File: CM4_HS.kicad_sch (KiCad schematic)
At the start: 6 parts, among them J1801 I2C EN, J1802 CM4/5 Module B

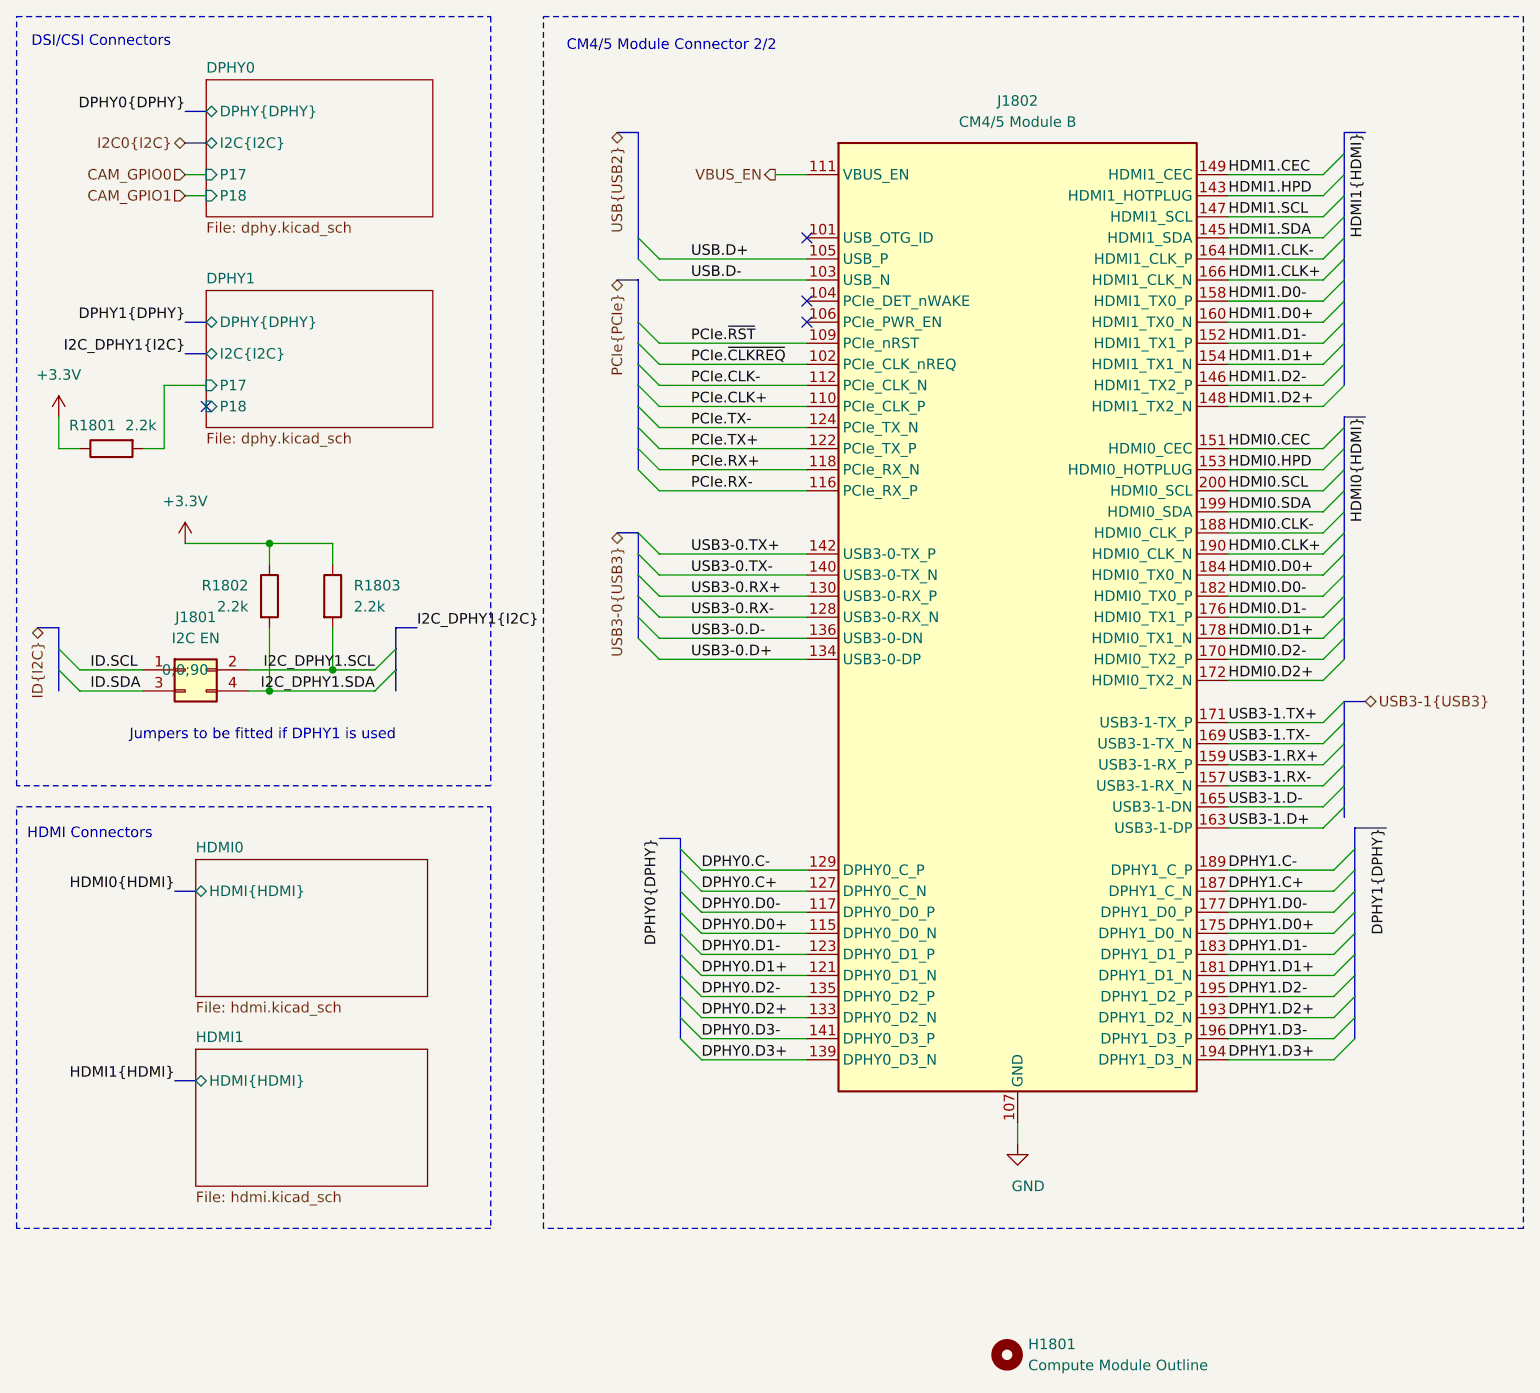
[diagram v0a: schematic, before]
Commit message: Replace DPHY selector jumper with a slide switch
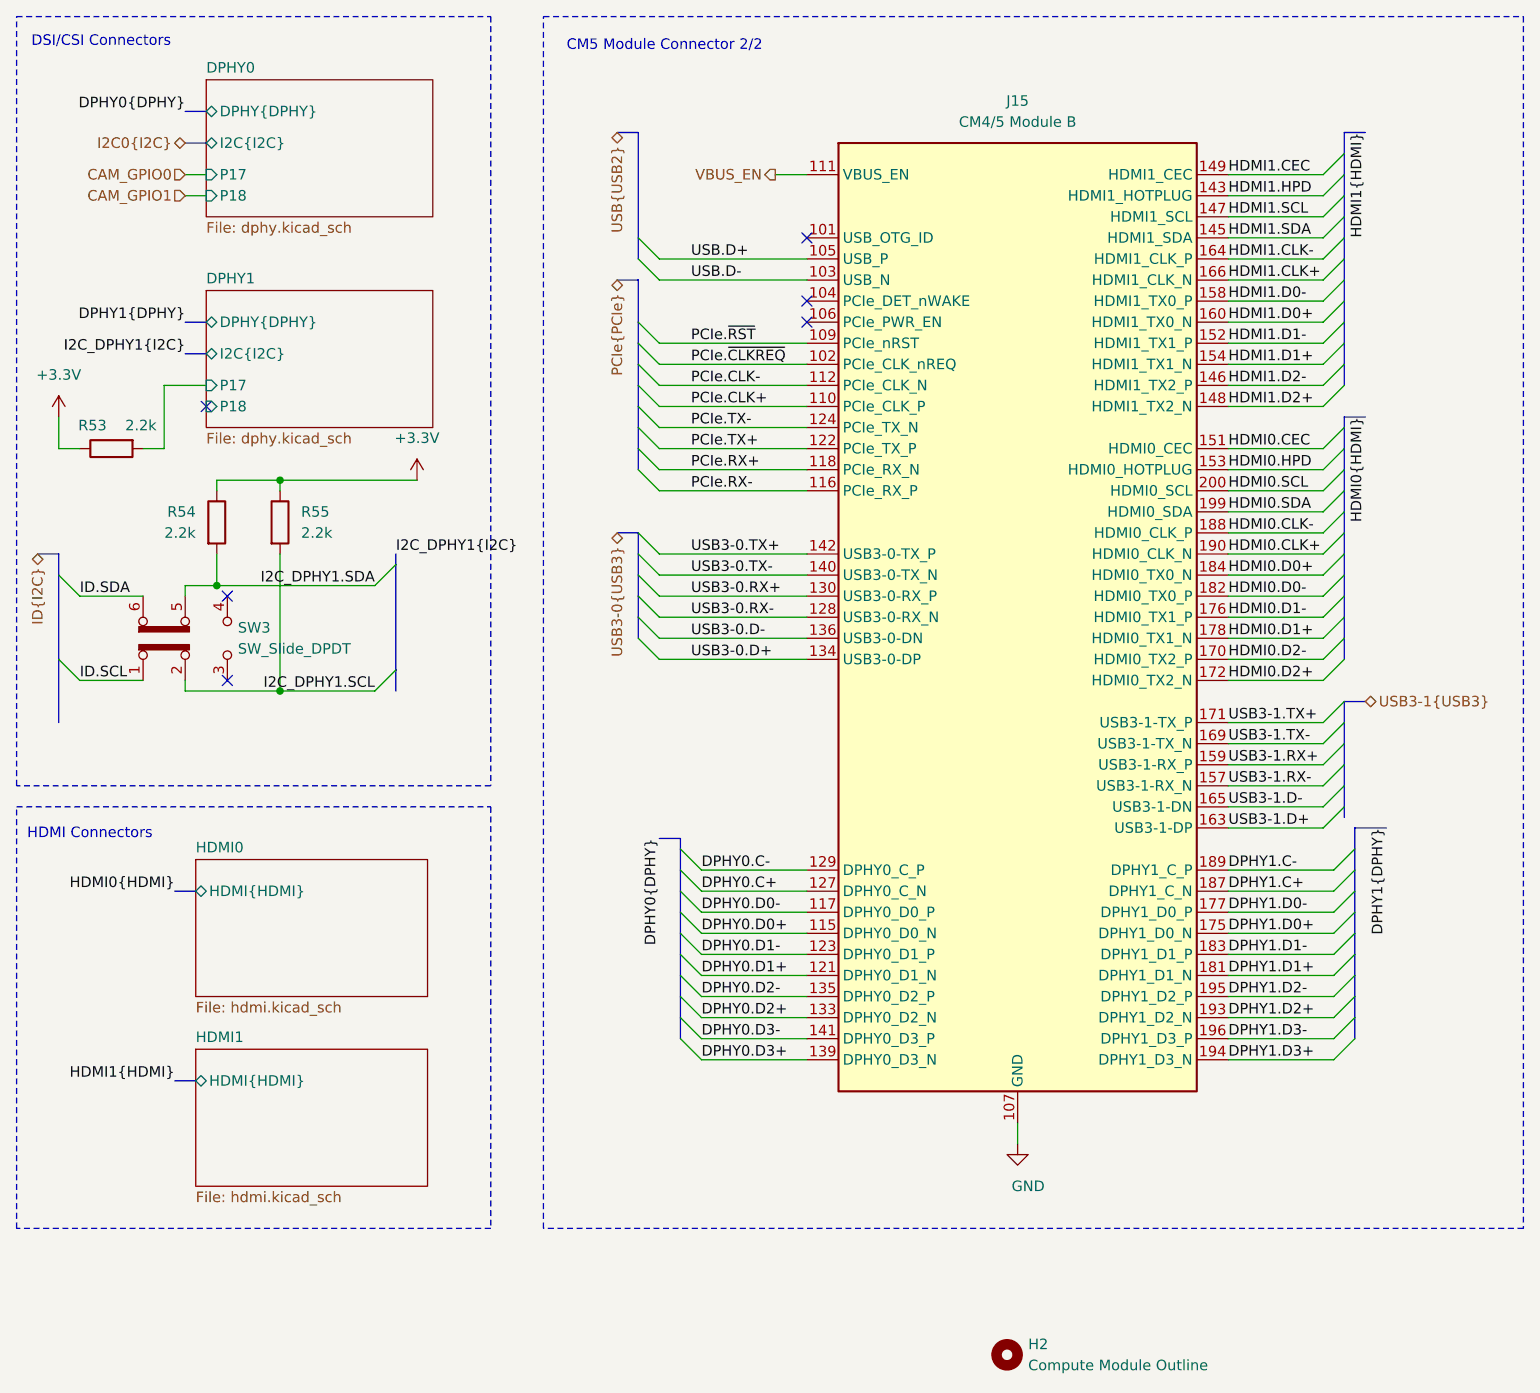
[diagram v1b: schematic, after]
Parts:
- removed J1801: I2C EN, Connector_PinHeader_2.54mm:PinHeader_2x02_P2.54mm_Vertical_SMD, symbol Connector_Generic:Conn_02x02_Odd_Even
- added SW3: SW_Slide_DPDT, HL_Button_Switch:SW-SMD_HX-MSS22C02-HXX-125, symbol Switch:SW_Slide_DPDT
- renumbered H1801 to H2, J1802 to J15, R1801 to R53, R1802 to R54, R1803 to R55
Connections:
- net I2C_DPHY1.SCL: now also SW3.2 (B)
- net I2C_DPHY1.SDA: now also SW3.5 (B)
- net ID.SCL: now also SW3.1 (A)
- net ID.SDA: now also SW3.6 (C)
- no-connect marks 4 -> 6
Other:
- note added: "CM5 Module Connector 2/2"
- note removed: "CM4/5 Module Connector 2/2"
- note removed: "Jumpers to be fitted if DPHY1 is used"
- moved on the sheet: R54, R55

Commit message: Reannotate the board
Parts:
- renumbered J15 to J14
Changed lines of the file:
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@@
+		(polyline
+			(pts
+				(xy 107.95 76.2) (xy 107.95 93.98) (xy 105.41 93.98) (xy 105.41 76.2)
+			)
+			(stroke
+				(width 0)
+				(type dash)
+			)
+			(fill
+				(type none)
+			)
+		)
+	)
+	(rule_area
 		(polyline
 			(pts
@@
 		(polyline
 			(pts
+				(xy 166.37 76.2) (xy 166.37 96.52) (xy 163.83 96.52) (xy 163.83 76.2)
+			)
+			(stroke
+				(width 0)
+				(type dash)
+			)
+			(fill
+				(type none)
+			)
+		)
+	)
+	(rule_area
+		(polyline
+			(pts
 				(xy 163.83 97.79) (xy 163.83 114.3) (xy 166.37 114.3) (xy 166.37 97.79)
+			)
+			(stroke
+				(width 0)
+				(type dash)
+			)
+			(fill
+				(type none)
+			)
+		)
+	)
+	(rule_area
+		(polyline
+			(pts
+				(xy 107.95 113.03) (xy 107.95 143.51) (xy 105.41 143.51) (xy 105.41 113.03)
+			)
+			(stroke
+				(width 0)
+				(type dash)
+			)
+			(fill
+				(type none)
+			)
+		)
+	)
+	(rule_area
+		(polyline
+			(pts
+				(xy 163.83 64.77) (xy 166.37 64.77) (xy 166.37 76.2) (xy 163.83 76.2)
+			)
+			(stroke
+				(width 0)
+				(type dash)
+			)
+			(fill
+				(type none)
+			)
+		)
+	)
+	(rule_area
+		(polyline
+			(pts
+				(xy 107.95 58.42) (xy 107.95 73.66) (xy 105.41 73.66) (xy 105.41 58.42)
 			)
 			(stroke
@@
 			(pts
 				(xy 105.41 53.34) (xy 107.95 53.34) (xy 107.95 58.42) (xy 105.41 58.42)
-			)
-			(stroke
-				(width 0)
-				(type dash)
-			)
-			(fill
-				(type none)
-			)
-		)
-	)
-	(rule_area
-		(polyline
-			(pts
-				(xy 163.83 64.77) (xy 166.37 64.77) (xy 166.37 76.2) (xy 163.83 76.2)
-			)
-			(stroke
-				(width 0)
-				(type dash)
-			)
-			(fill
-				(type none)
-			)
-		)
-	)
-	(rule_area
-		(polyline
-			(pts
-				(xy 107.95 76.2) (xy 107.95 93.98) (xy 105.41 93.98) (xy 105.41 76.2)
-			)
-			(stroke
-				(width 0)
-				(type dash)
-			)
-			(fill
-				(type none)
-			)
-		)
-	)
-	(rule_area
-		(polyline
-			(pts
-				(xy 107.95 113.03) (xy 107.95 143.51) (xy 105.41 143.51) (xy 105.41 113.03)
-			)
-			(stroke
-				(width 0)
-				(type dash)
-			)
-			(fill
-				(type none)
-			)
-		)
-	)
-	(rule_area
-		(polyline
-			(pts
-				(xy 107.95 58.42) (xy 107.95 73.66) (xy 105.41 73.66) (xy 105.41 58.42)
-			)
-			(stroke
-				(width 0)
-				(type dash)
-			)
-			(fill
-				(type none)
-			)
-		)
-	)
-	(rule_area
-		(polyline
-			(pts
-				(xy 166.37 76.2) (xy 166.37 96.52) (xy 163.83 96.52) (xy 163.83 76.2)
 			)
 			(stroke
@@
 		(dnp no)
 		(fields_autoplaced yes)
-		(property "Reference" "#PWR0108"
+		(property "Reference" "#PWR0107"
 			(at 20.32 67.31 0)
 			(effects
@@
 			(project ""
 				(path "/abc482bd-3f17-4d35-80db-1da3dcdb5c27/851e7ce4-d5b0-47f7-ace9-4a347f172348"
-					(reference "#PWR0108")
+					(reference "#PWR0107")
 					(unit 1)
 				)
@@
 		(on_board yes)
 		(dnp no)
-		(property "Reference" "#PWR0110"
+		(property "Reference" "#PWR0109"
 			(at 135.89 157.48 0)
 			(effects
@@
 			(project "Yellow"
 				(path "/abc482bd-3f17-4d35-80db-1da3dcdb5c27/851e7ce4-d5b0-47f7-ace9-4a347f172348"
-					(reference "#PWR0110")
+					(reference "#PWR0109")
 					(unit 1)
 				)
@@
 		(dnp no)
 		(fields_autoplaced yes)
-		(property "Reference" "J15"
+		(property "Reference" "J14"
 			(at 135.89 25.4 0)
 			(effects
@@
 			(project ""
 				(path "/abc482bd-3f17-4d35-80db-1da3dcdb5c27/851e7ce4-d5b0-47f7-ace9-4a347f172348"
-					(reference "J15")
+					(reference "J14")
 					(unit 1)
 				)
@@
 		(dnp no)
 		(fields_autoplaced yes)
-		(property "Reference" "#PWR0109"
+		(property "Reference" "#PWR0108"
 			(at 63.5 74.93 0)
 			(effects
@@
 			(project "HALPI2"
 				(path "/abc482bd-3f17-4d35-80db-1da3dcdb5c27/851e7ce4-d5b0-47f7-ace9-4a347f172348"
-					(reference "#PWR0109")
+					(reference "#PWR0108")
 					(unit 1)
 				)

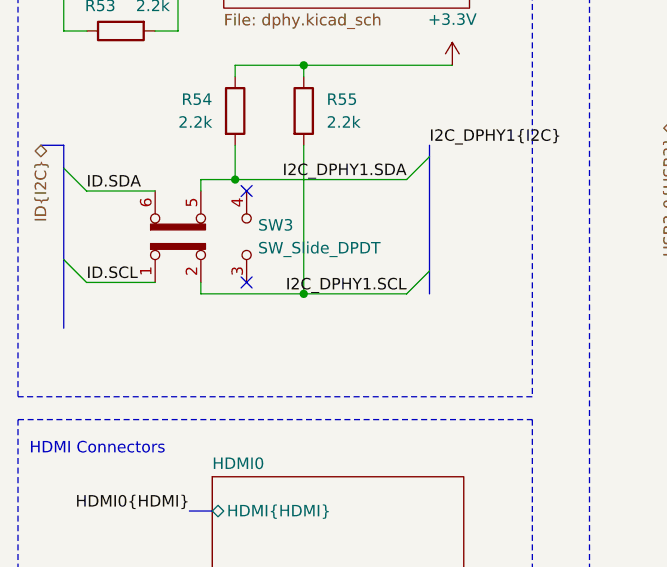
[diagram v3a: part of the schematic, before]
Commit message: Add GND/3.3V/5V headers, add missing JLC part numbers
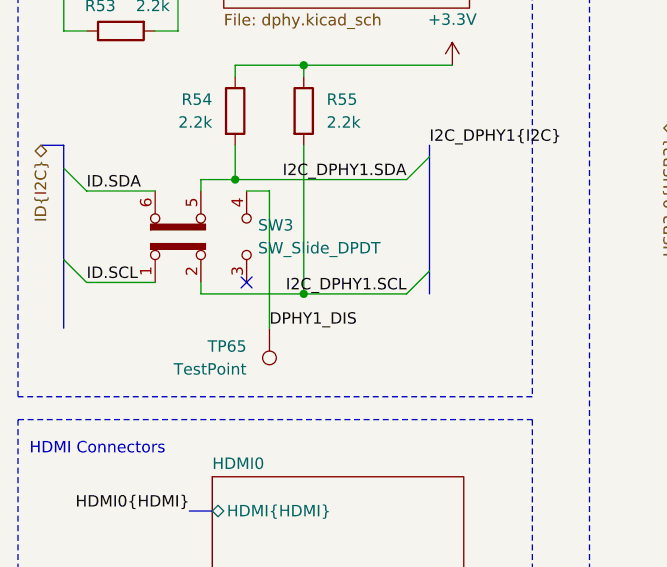
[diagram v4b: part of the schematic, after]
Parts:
- added TP65: TestPoint, TestPoint:TestPoint_Pad_D1.0mm, symbol Connector:TestPoint
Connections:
- net DPHY1_DIS: now reaches SW3.4 (A)
- net DPHY1_DIS: now also TP65.1
- no-connect marks 6 -> 5
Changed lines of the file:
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@@
 	)
 	(no_connect
-		(at 40.64 85.09)
-	)
-	(no_connect
 		(at 40.64 95.25)
 	)
@@
 		)
 	)
+	(wire
+		(pts
+			(xy 43.18 85.09) (xy 40.64 85.09)
+		)
+		(stroke
+			(width 0)
+			(type default)
+		)
+	)
 	(polyline
 		(pts
@@
 	(wire
 		(pts
+			(xy 43.18 100.33) (xy 43.18 85.09)
+		)
+		(stroke
+			(width 0)
+			(type default)
+		)
+	)
+	(wire
+		(pts
 			(xy 161.29 59.69) (xy 172.72 59.69)
 		)
@@
 		)
 	)
+	(label "DPHY1_DIS"
+		(at 43.18 100.33 0)
+		(effects
+			(font
+				(size 1.27 1.27)
+			)
+			(justify left bottom)
+		)
+	)
 	(label "HDMI0{HDMI}"
 		(at 177.8 63.5 270)
@@
 					(unit 1)
 				)
+			)
+		)
+	)
+	(symbol
+		(lib_id "Connector:TestPoint")
+		(at 43.18 100.33 0)
+		(mirror x)
+		(unit 1)
+		(exclude_from_sim no)
+		(in_bom yes)
+		(on_board yes)
+		(dnp no)
+		(fields_autoplaced yes)
+		(property "Reference" "TP65"
+			(at 40.64 102.3619 0)
+			(effects
+				(font
+					(size 1.27 1.27)
+				)
+				(justify right)
+			)
+		)
+		(property "Value" "TestPoint"
+			(at 40.64 104.9019 0)
+			(effects
+				(font
+					(size 1.27 1.27)
+				)
+				(justify right)
+			)
+		)
+		(property "Footprint" "TestPoint:TestPoint_Pad_D1.0mm"
+			(at 48.26 100.33 0)
+			(effects
+				(font
+					(size 1.27 1.27)
+				)
+				(hide yes)
+			)
+		)
+		(property "Datasheet" "~"
+			(at 48.26 100.33 0)
+			(effects
+				(font
+					(size 1.27 1.27)
+				)
+				(hide yes)
+			)
+		)
+		(property "Description" "test point"
+			(at 43.18 100.33 0)
+			(effects
+				(font
+					(size 1.27 1.27)
+				)
+				(hide yes)
+			)
+		)
+		(property "Characteristics" ""
+			(at 43.18 100.33 0)
+			(effects
+				(font
+					(size 1.27 1.27)
+				)
+				(hide yes)
+			)
+		)
+		(property "LCSC Part" ""
+			(at 43.18 100.33 0)
+			(effects
+				(font
+					(size 1.27 1.27)
+				)
+			)
+		)
+		(property "Field8" ""
+			(at 43.18 100.33 0)
+			(effects
+				(font
+					(size 1.27 1.27)
+				)
+			)
+		)
+		(property "PartNumber" ""
+			(at 43.18 100.33 0)
+			(effects
+				(font
+					(size 1.27 1.27)
+				)
+			)
+		)
+		(pin "1"
+		)
+		(instances
+			(project "HALPI2"
+				(path "/abc482bd-3f17-4d35-80db-1da3dcdb5c27/851e7ce4-d5b0-47f7-ace9-4a347f172348"
+					(reference "TP65")
+					(unit 1)
+				)

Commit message: FInal v0.2.0 proto changes
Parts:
- renumbered TP65 to TP35
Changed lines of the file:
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@@
+		(polyline
+			(pts
+				(xy 163.83 31.75) (xy 166.37 31.75) (xy 166.37 43.18) (xy 163.83 43.18)
+			)
+			(stroke
+				(width 0)
+				(type dash)
+			)
+			(fill
+				(type none)
+			)
+		)
+	)
+	(rule_area
 		(polyline
 			(pts
 				(xy 107.95 43.18) (xy 107.95 48.26) (xy 105.41 48.26) (xy 105.41 43.18)
+			)
+			(stroke
+				(width 0)
+				(type dash)
+			)
+			(fill
+				(type none)
+			)
+		)
+	)
+	(rule_area
+		(polyline
+			(pts
+				(xy 107.95 76.2) (xy 107.95 93.98) (xy 105.41 93.98) (xy 105.41 76.2)
 			)
 			(stroke
@@
 		(polyline
 			(pts
-				(xy 107.95 76.2) (xy 107.95 93.98) (xy 105.41 93.98) (xy 105.41 76.2)
+				(xy 166.37 76.2) (xy 166.37 96.52) (xy 163.83 96.52) (xy 163.83 76.2)
 			)
 			(stroke
@@
 		(polyline
 			(pts
-				(xy 163.83 142.24) (xy 163.83 115.57) (xy 166.37 115.57) (xy 166.37 142.24)
+				(xy 166.37 43.18) (xy 166.37 63.5) (xy 163.83 63.5) (xy 163.83 43.18)
 			)
 			(stroke
@@
 		(polyline
 			(pts
-				(xy 163.83 31.75) (xy 166.37 31.75) (xy 166.37 43.18) (xy 163.83 43.18)
+				(xy 57.15 97.79) (xy 54.61 97.79) (xy 54.61 82.55) (xy 57.15 82.55)
+			)
+			(stroke
+				(width 0)
+				(type dash)
+			)
+			(fill
+				(type none)
+			)
+		)
+	)
+	(rule_area
+		(polyline
+			(pts
+				(xy 163.83 97.79) (xy 163.83 114.3) (xy 166.37 114.3) (xy 166.37 97.79)
 			)
 			(stroke
@@
 		(polyline
 			(pts
-				(xy 166.37 76.2) (xy 166.37 96.52) (xy 163.83 96.52) (xy 163.83 76.2)
+				(xy 107.95 58.42) (xy 107.95 73.66) (xy 105.41 73.66) (xy 105.41 58.42)
 			)
 			(stroke
@@
 		(polyline
 			(pts
-				(xy 166.37 43.18) (xy 166.37 63.5) (xy 163.83 63.5) (xy 163.83 43.18)
-			)
-			(stroke
-				(width 0)
-				(type dash)
-			)
-			(fill
-				(type none)
-			)
-		)
-	)
-	(rule_area
-		(polyline
-			(pts
-				(xy 57.15 97.79) (xy 54.61 97.79) (xy 54.61 82.55) (xy 57.15 82.55)
-			)
-			(stroke
-				(width 0)
-				(type dash)
-			)
-			(fill
-				(type none)
-			)
-		)
-	)
-	(rule_area
-		(polyline
-			(pts
-				(xy 107.95 58.42) (xy 107.95 73.66) (xy 105.41 73.66) (xy 105.41 58.42)
-			)
-			(stroke
-				(width 0)
-				(type dash)
-			)
-			(fill
-				(type none)
-			)
-		)
-	)
-	(rule_area
-		(polyline
-			(pts
-				(xy 163.83 97.79) (xy 163.83 114.3) (xy 166.37 114.3) (xy 166.37 97.79)
+				(xy 163.83 142.24) (xy 163.83 115.57) (xy 166.37 115.57) (xy 166.37 142.24)
 			)
 			(stroke
@@
 		(dnp no)
 		(fields_autoplaced yes)
-		(property "Reference" "#PWR0107"
+		(property "Reference" "#PWR0108"
 			(at 20.32 67.31 0)
 			(effects
@@
 			(project ""
 				(path "/abc482bd-3f17-4d35-80db-1da3dcdb5c27/851e7ce4-d5b0-47f7-ace9-4a347f172348"
-					(reference "#PWR0107")
+					(reference "#PWR0108")
 					(unit 1)
 				)
@@
 		(dnp no)
 		(fields_autoplaced yes)
-		(property "Reference" "TP65"
+		(property "Reference" "TP35"
 			(at 40.64 102.3619 0)
 			(effects
@@
 		)
 		(property "PartNumber" ""
+			(at 43.18 100.33 0)
+			(effects
+				(font
+					(size 1.27 1.27)
+				)
+			)
+		)
+		(property "Sim.Enable" ""
 			(at 43.18 100.33 0)
 			(effects
@@
 			(project "HALPI2"
 				(path "/abc482bd-3f17-4d35-80db-1da3dcdb5c27/851e7ce4-d5b0-47f7-ace9-4a347f172348"
-					(reference "TP65")
+					(reference "TP35")
 					(unit 1)
 				)
@@
 		(on_board yes)
 		(dnp no)
-		(property "Reference" "#PWR0109"
+		(property "Reference" "#PWR0110"
 			(at 135.89 157.48 0)
 			(effects
@@
 			(project "Yellow"
 				(path "/abc482bd-3f17-4d35-80db-1da3dcdb5c27/851e7ce4-d5b0-47f7-ace9-4a347f172348"
-					(reference "#PWR0109")
+					(reference "#PWR0110")
 					(unit 1)
 				)
@@
 		(dnp no)
 		(fields_autoplaced yes)
-		(property "Reference" "#PWR0108"
+		(property "Reference" "#PWR0109"
 			(at 63.5 74.93 0)
 			(effects
@@
 			(project "HALPI2"
 				(path "/abc482bd-3f17-4d35-80db-1da3dcdb5c27/851e7ce4-d5b0-47f7-ace9-4a347f172348"
-					(reference "#PWR0108")
+					(reference "#PWR0109")
 					(unit 1)
 				)
